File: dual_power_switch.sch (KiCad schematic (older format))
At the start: 1 part

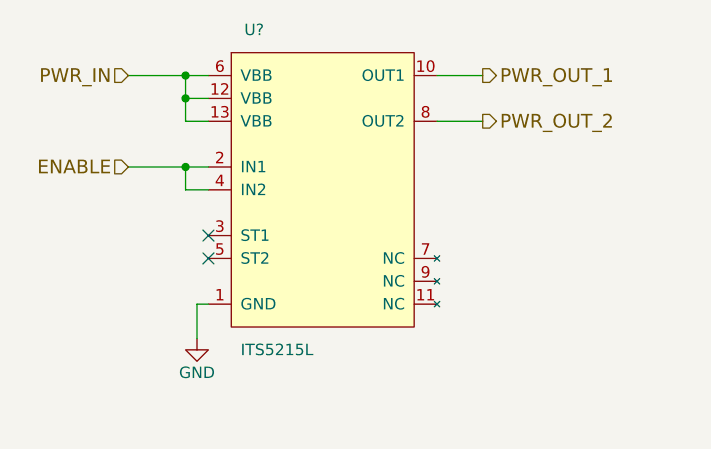
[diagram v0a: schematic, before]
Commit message: add 5v power switch
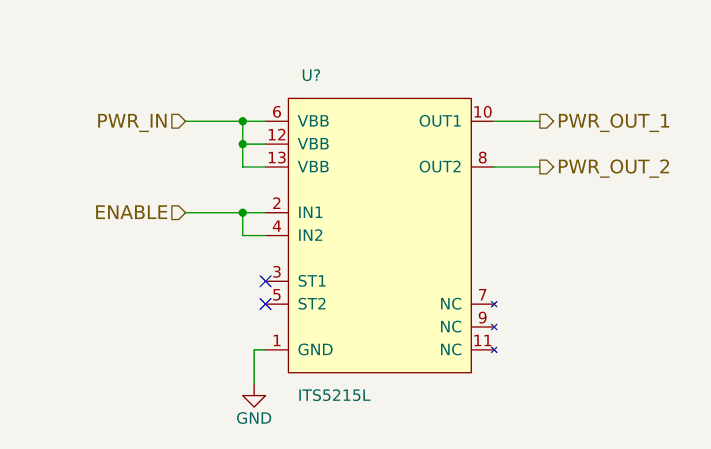
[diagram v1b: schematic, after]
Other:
- moved on the sheet: U?
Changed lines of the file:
@@
 $Descr A4 11693 8268
 encoding utf-8
-Sheet 5 6
+Sheet 5 7
 Title ""
 Date ""
@@
 L ITS5215L U?
 U 1 1 59613FBB
-P 5800 3600
-F 0 "U?" H 5500 4300 50  0000 C CNN
-F 1 "ITS5215L" H 5600 2900 50  0000 C CNN
-F 2 "" H 6900 2600 50  0001 C CNN
-F 3 "" H 6900 2600 50  0001 C CNN
-	1    5800 3600
+P 6050 3800
+F 0 "U?" H 5750 4500 50  0000 C CNN
+F 1 "ITS5215L" H 5850 3100 50  0000 C CNN
+F 2 "" H 7150 2800 50  0001 C CNN
+F 3 "" H 7150 2800 50  0001 C CNN
+	1    6050 3800
 	1    0    0    -1
 $EndComp
 Wire Wire Line
-	5300 3300 5200 3300
+	5550 3500 5450 3500
 Wire Wire Line
-	5200 3300 5200 3100
+	5450 3500 5450 3300
 Wire Wire Line
-	4950 3100 5300 3100
-Connection ~ 5200 3100
+	5200 3300 5550 3300
+Connection ~ 5450 3300
 Wire Wire Line
-	5300 3200 5200 3200
-Connection ~ 5200 3200
+	5550 3400 5450 3400
+Connection ~ 5450 3400
 Wire Wire Line
-	4950 3500 5300 3500
+	5200 3700 5550 3700
 Wire Wire Line
-	5300 3600 5200 3600
-NoConn ~ 5300 3800
-NoConn ~ 5300 3900
+	5550 3800 5450 3800
+NoConn ~ 5550 4000
+NoConn ~ 5550 4100
 Wire Wire Line
-	5300 4100 5250 4100
+	5550 4300 5500 4300
 Wire Wire Line
-	5250 4100 5250 4250
+	5500 4300 5500 4450
 $Comp
 L GND #PWR?
 U 1 1 59614225
-P 5250 4250
-F 0 "#PWR?" H 5250 4000 50  0001 C CNN
-F 1 "GND" H 5250 4100 50  0000 C CNN
-F 2 "" H 5250 4250 50  0001 C CNN
-F 3 "" H 5250 4250 50  0001 C CNN
-	1    5250 4250
+P 5500 4450
+F 0 "#PWR?" H 5500 4200 50  0001 C CNN
+F 1 "GND" H 5500 4300 50  0000 C CNN
+F 2 "" H 5500 4450 50  0001 C CNN
+F 3 "" H 5500 4450 50  0001 C CNN
+	1    5500 4450
 	1    0    0    -1
 $EndComp
 Wire Wire Line
-	6300 3100 6500 3100
+	6550 3300 6750 3300
 Wire Wire Line
-	6300 3300 6500 3300
-Text HLabel 4950 3100 0    60   Input ~ 0
+	6550 3500 6750 3500
+Text HLabel 5200 3300 0    60   Input ~ 0
 PWR_IN
-Text HLabel 4950 3500 0    60   Input ~ 0
+Text HLabel 5200 3700 0    60   Input ~ 0
 ENABLE
 Wire Wire Line
-	5200 3600 5200 3500
-Connection ~ 5200 3500
-Text HLabel 6500 3100 2    60   Output ~ 0
+	5450 3800 5450 3700
+Connection ~ 5450 3700
+Text HLabel 6750 3300 2    60   Output ~ 0
 PWR_OUT_1
-Text HLabel 6500 3300 2    60   Output ~ 0
+Text HLabel 6750 3500 2    60   Output ~ 0
 PWR_OUT_2
 $EndSCHEMATC

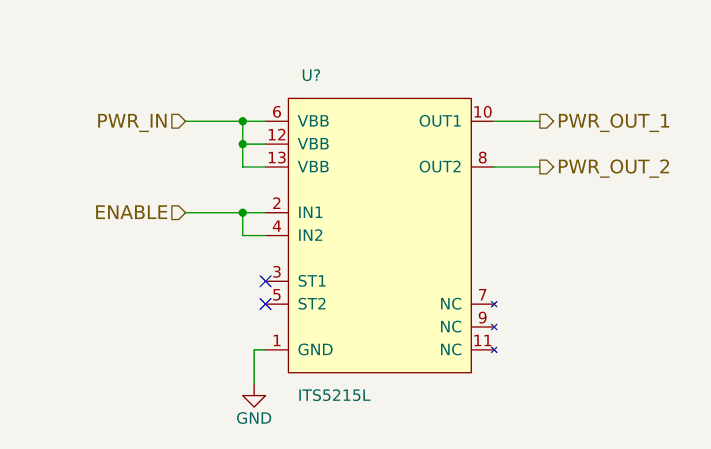
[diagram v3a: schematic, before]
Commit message: power switches connect to pgnd
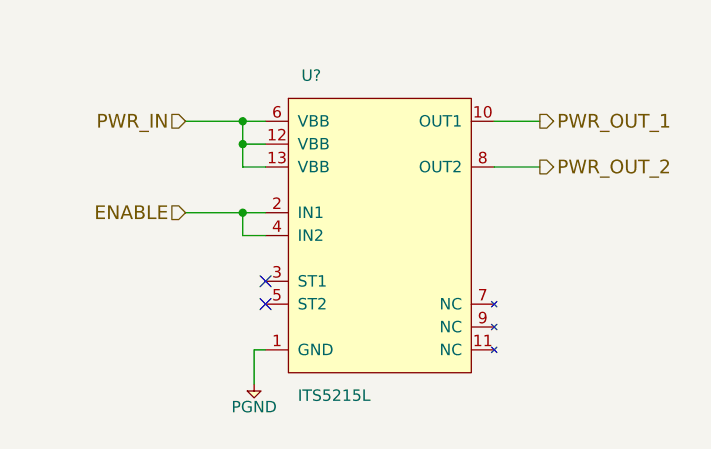
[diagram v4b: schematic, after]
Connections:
- net GND renamed PGND
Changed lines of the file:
@@
 Wire Wire Line
 	5500 4300 5500 4450
-$Comp
-L GND #PWR?
-U 1 1 59614225
-P 5500 4450
-AR Path="/5957D255/59613F99/59614225" Ref="#PWR?"  Part="1"
-AR Path="/5957D255/5961B13A/59614225" Ref="#PWR?"  Part="1"
-F 0 "#PWR?" H 5500 4200 50  0001 C CNN
-F 1 "GND" H 5500 4300 50  0000 C CNN
-F 2 "" H 5500 4450 50  0001 C CNN
-F 3 "" H 5500 4450 50  0001 C CNN
-	1    5500 4450
-	1    0    0    -1
-$EndComp
 Wire Wire Line
 	6550 3300 6750 3300
@@
 Text HLabel 6750 3500 2    60   Output ~ 0
 PWR_OUT_2
+$Comp
+L PGND #PWR?
+U 1 1 5962B650
+P 5500 4450
+F 0 "#PWR?" H 5370 4490 50  0001 L CNN
+F 1 "PGND" H 5500 4350 50  0000 C CNN
+F 2 "" H 5500 4450 60  0001 C CNN
+F 3 "" H 5500 4450 60  0001 C CNN
+	1    5500 4450
+	1    0    0    -1
+$EndComp
 $EndSCHEMATC

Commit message: clean up after annotate
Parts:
- gave numbers to parts that had none: 1
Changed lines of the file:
@@
 $EndDescr
 $Comp
-L ITS5215L U?
+L ITS5215L U3
 U 1 1 59613FBB
 P 6050 3800
-AR Path="/5957D255/59613F99/59613FBB" Ref="U?"  Part="1"
+AR Path="/5957D255/59613F99/59613FBB" Ref="U3"  Part="1"
 AR Path="/5957D255/5961B13A/59613FBB" Ref="U?"  Part="1"
-F 0 "U?" H 5750 4500 50  0000 C CNN
+F 0 "U3" H 5750 4500 50  0000 C CNN
 F 1 "ITS5215L" H 5850 3100 50  0000 C CNN
 F 2 "" H 7150 2800 50  0001 C CNN
@@
 PWR_OUT_2
 $Comp
-L PGND #PWR?
+L PGND #PWR13
 U 1 1 5962B650
 P 5500 4450
-F 0 "#PWR?" H 5370 4490 50  0001 L CNN
+F 0 "#PWR13" H 5370 4490 50  0001 L CNN
 F 1 "PGND" H 5500 4350 50  0000 C CNN
 F 2 "" H 5500 4450 60  0001 C CNN
